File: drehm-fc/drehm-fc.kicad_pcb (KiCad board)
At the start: 2 copper layers, 18 parts, among them J1 TSW-113-08-T-T-RA, J4 Conn_01x04, U1 DEV-15583

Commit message: design rules set, teensy footprint modified
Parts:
- removed TP1, TP2: TestPoint, TestPoint:TestPoint_Pad_4.0x4.0mm
- J4: footprint Connector_PinHeader_2.54mm:PinHeader_1x04_P2.54mm_Horizontal -> Connector_PinHeader_2.54mm:PinHeader_1x04_P2.54mm_Vertical
- moved MT1 51.9 mm to (152.1, 122.2), turned to 180 degrees
- moved R1 42.7 mm to (151.7, 124.2)
- moved C2 42.0 mm to (153.9, 119.6), turned to 90 degrees
- moved R2 41.7 mm to (153.2, 124.7), turned to 180 degrees
- moved C3 40.5 mm to (154.7, 119.6), turned to 90 degrees
- moved C1 36.6 mm to (152.8, 112.5), turned to 180 degrees
- moved J1 17.3 mm to (127.7, 126.4), turned to -90 degrees
- moved J4 15.6 mm to (159.2, 113.7)
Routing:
- net /UART RX/I2C SCL: track 0.00 -> 20.9 mm
- net /UART TX/I2C SDA: track 0.00 -> 15.2 mm
- net +3V3: track 0.00 -> 3.12 mm

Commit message: IMU Routing finished, board outline done
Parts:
- moved H1 80.5 mm to (125.0, 147.0)
- moved FID1 70.5 mm to (129.5, 147.0)
- moved H3 69.0 mm to (159.0, 147.0)
- moved H2 36.1 mm to (159.0, 103.0)
- moved FID2 25.0 mm to (154.5, 103.0)
- moved FID3 22.2 mm to (129.5, 103.0)
- moved H4 18.4 mm to (125.0, 103.0)
- moved C1 14.9 mm to (150.1, 127.2), turned to 90 degrees
- moved C3 12.1 mm to (151.0, 131.1), turned to 180 degrees
- moved C2 11.1 mm to (151.0, 130.3), turned to 180 degrees
- moved MT1 5.87 mm to (152.0, 128.0), turned to -90 degrees
- moved R1 4.76 mm to (154.0, 128.4), turned to 90 degrees
- moved J1 2.33 mm to (130.0, 126.4)
- moved R2 2.30 mm to (154.0, 126.9), turned to -90 degrees
- moved J4 0.25 mm to (159.5, 113.7)
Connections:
- J1 pad 36: (no net) -> Net-(J1-Pad36)
- J1 pad 39: (no net) -> Net-(J1-Pad39)
- U1 pad 11: Net-(J1A-36) -> Net-(J1-Pad36)
- U1 pad 12: Net-(J1A-39) -> Net-(J1-Pad39)
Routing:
- net /+5V: track 0.00 -> 56.4 mm
- net +3V3: track 3.12 -> 56.3 mm
- net INT2: track 0.00 -> 20.0 mm, vias 0 -> 2
- net INT1: track 0.00 -> 13.5 mm
- net /IMU_SDA: track 0.00 -> 10.7 mm
- net Earth: track 0.00 -> 6.84 mm, vias 0 -> 6
- net Net-(J1-Pad39): track 0.00 -> 3.09 mm
- net Net-(J1-Pad36): track 0.00 -> 3.09 mm
- net Net-(J1-Pad33): track 0.00 -> 3.09 mm
- net Net-(J1-Pad30): track 0.00 -> 3.09 mm
- net Net-(J1-Pad27): track 0.00 -> 3.09 mm
- net Net-(J1-Pad24): track 0.00 -> 3.09 mm
- net Net-(J1-Pad21): track 0.00 -> 3.09 mm
- net Net-(J1-Pad18): track 0.00 -> 3.09 mm
- net Net-(J1-Pad15): track 0.00 -> 3.09 mm
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- added copper zone on F.Cu, net +3V3
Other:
- board outline added: 40.5 x 50.5 mm

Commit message: Routing mostly done, finishing touches WIP
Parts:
- moved J4 36.7 mm to (140.9, 145.3), turned to 90 degrees
- moved H3 3.48 mm to (155.6, 146.6)
- moved FID2 3.45 mm to (151.1, 103.0)
- moved H2 3.45 mm to (155.6, 103.0)
- moved FID1 0.90 mm to (130.2, 146.5)
- moved H1 0.90 mm to (125.8, 146.5)
- moved FID3 0.75 mm to (130.2, 103.0)
- moved H4 0.75 mm to (125.8, 103.0)
- moved C3 0.06 mm to (151.0, 131.2)
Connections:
- J1 pad 01: Net-(J1-Pad01) -> Earth
- J1 pad 04: Net-(J1-Pad01) -> Earth
- J1 pad 07: Net-(J1-Pad01) -> Earth
- J1 pad 10: Net-(J1-Pad01) -> Earth
- J1 pad 13: Net-(J1-Pad01) -> Earth
- J1 pad 16: Net-(J1-Pad01) -> Earth
- J1 pad 19: Net-(J1-Pad01) -> Earth
- J1 pad 22: Net-(J1-Pad01) -> Earth
- J1 pad 25: Net-(J1-Pad01) -> Earth
- J1 pad 28: Net-(J1-Pad01) -> Earth
- J1 pad 31: Net-(J1-Pad01) -> Earth
- J1 pad 34: Net-(J1-Pad01) -> Earth
- J1 pad 37: Net-(J1-Pad01) -> Earth
- U1 pad G1: Net-(J1-Pad01) -> Earth
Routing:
- net +3V3: track 56.3 -> 73.1 mm
- net Earth: track 6.84 -> 22.8 mm, vias 6 -> 19
- net /UART TX/I2C SDA: track 16.2 -> 18.0 mm
- net /IMU_SCL: track 2.81 -> 3.90 mm
- net /UART RX/I2C SCL: track 21.1 -> 22.1 mm
- added copper zone on B.Cu, net Earth
- added copper zone on F.Cu, net Earth
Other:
- board size 40.5 x 50.5 mm -> 36.3 x 50 mm
- board text added: "+"
- board text added: "+3.3v"
- board text added: "+5V"
- board text added: "-"
- board text added: "GND"

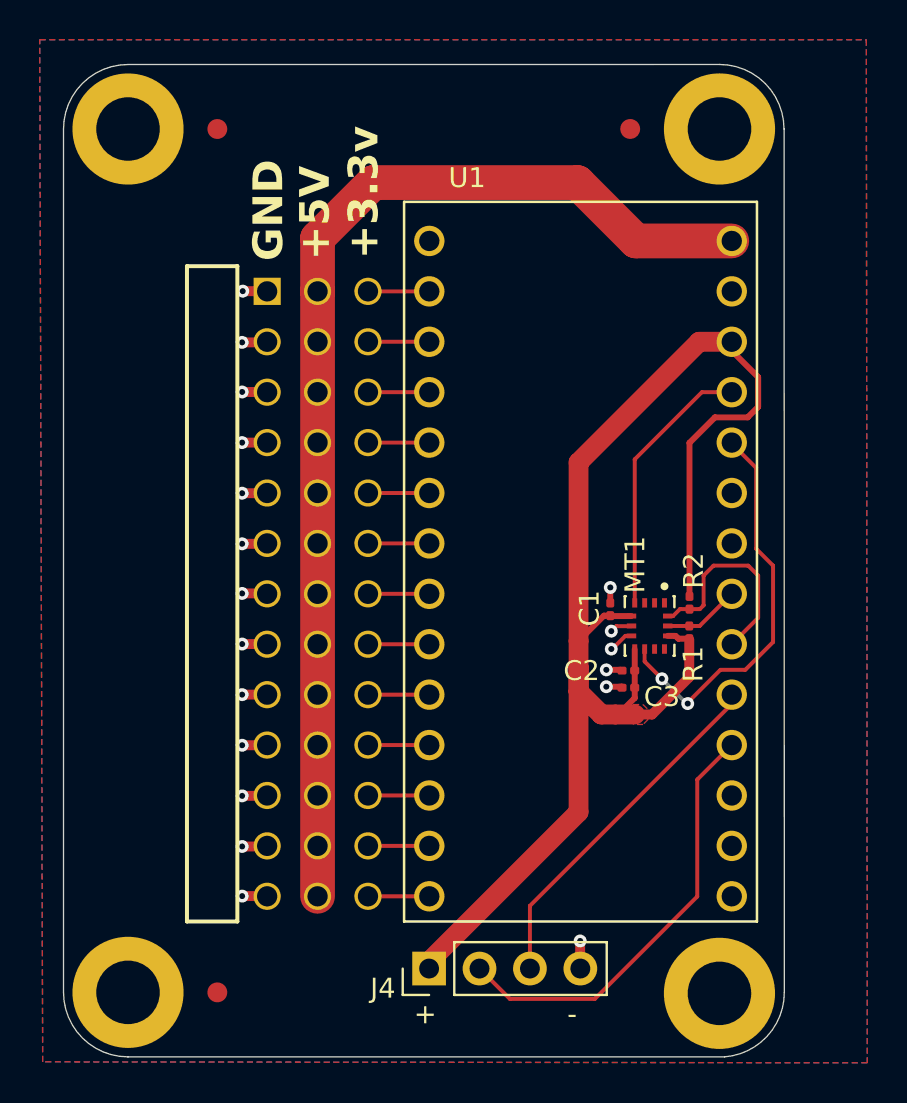
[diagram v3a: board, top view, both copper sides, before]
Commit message: Manufacturability changes, silkscreen update
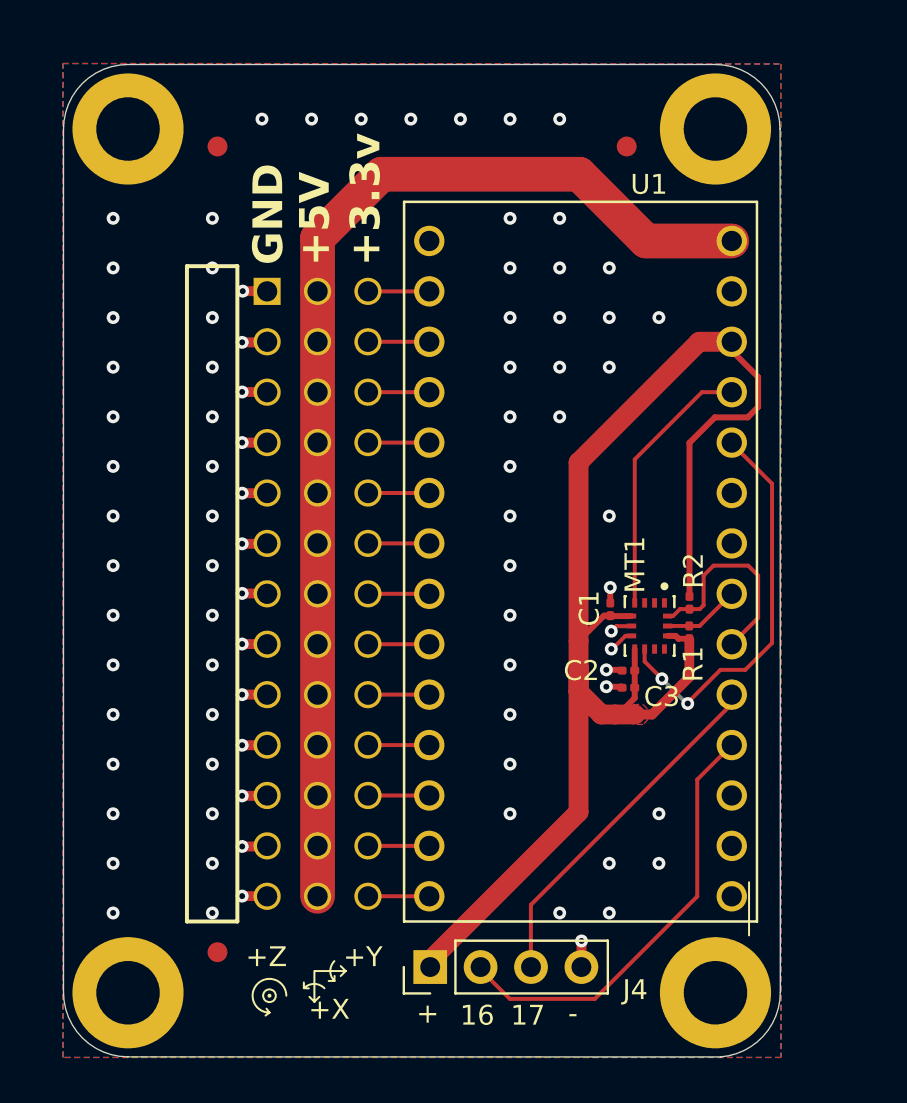
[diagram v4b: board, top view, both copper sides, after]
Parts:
- moved FID1 2.02 mm to (130.3, 144.5)
- moved FID2 0.90 mm to (150.9, 103.9)
- moved FID3 0.88 mm to (130.3, 103.9)
- moved H3 0.20 mm to (155.3, 146.5)
- moved H2 0.20 mm to (155.3, 103.0)
- moved J4 0.09 mm to (141.0, 145.2)
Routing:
- net Earth: vias 19 -> 84
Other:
- board size 36.3 x 50 mm -> 36.1 x 50 mm
- board text added: "+X"
- board text added: "+Y"
- board text added: "+Z"
- board text added: "16"
- board text added: "17"
- board text added: "{ "ViaStitching": "0.2", "stitch_zone_0": { "HSpacing": ".5", "VSpacing": ".5", "Clearance": "0", "Randomize": false } }"
- board text added: "{ "ViaStitching": "0.2", "stitch_zone_0": { "HSpacing": "1", "VSpacing": "1", "Clearance": "0", "Randomize": false } }"

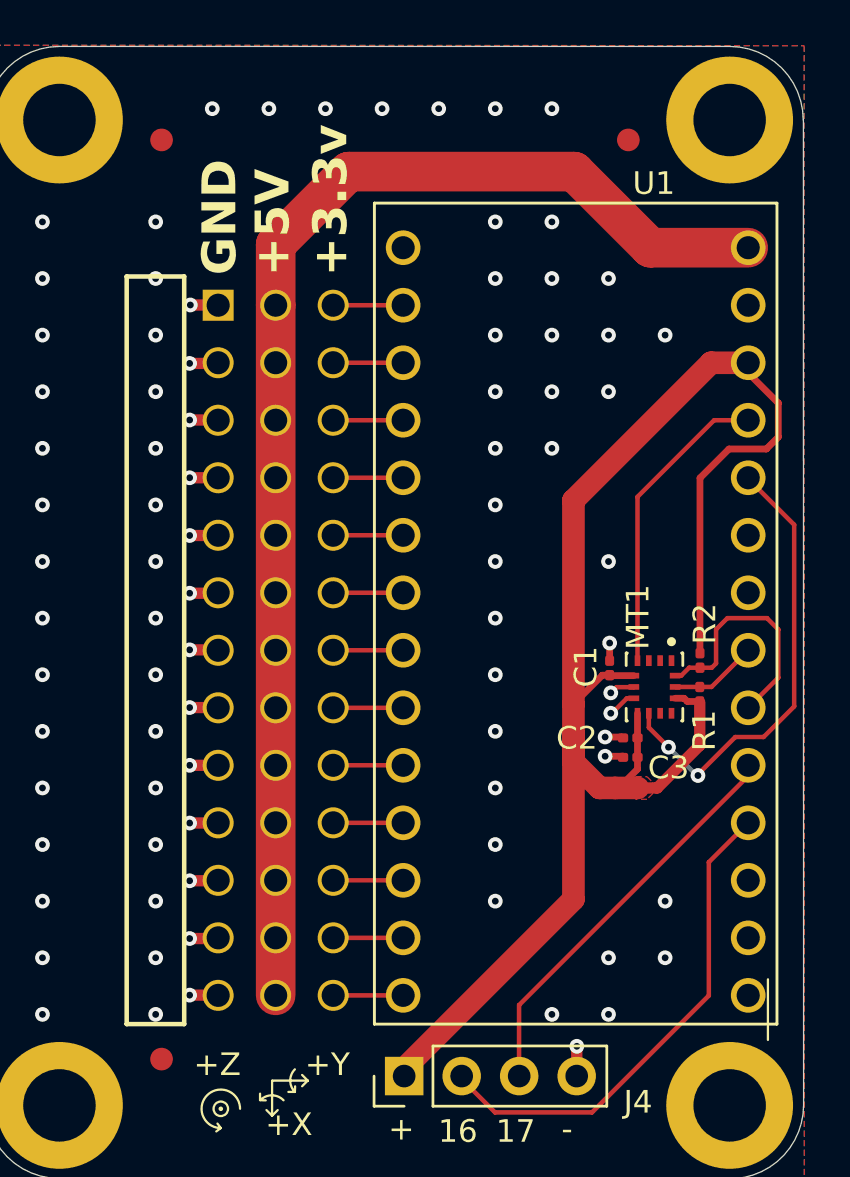
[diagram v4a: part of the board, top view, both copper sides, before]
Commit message: name and rev on silkscreen
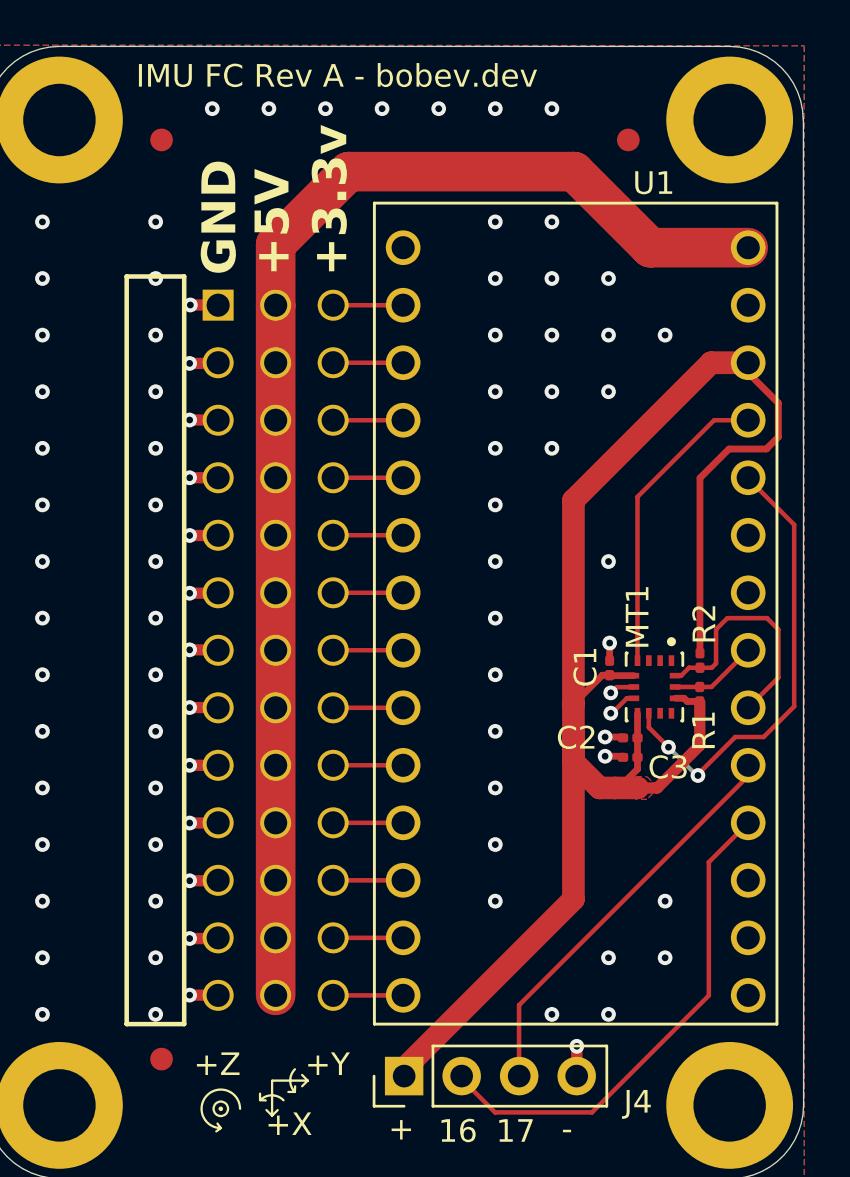
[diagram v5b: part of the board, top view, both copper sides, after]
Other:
- board text added: "IMU FC Rev A - bobev.dev"
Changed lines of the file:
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@@
-		(layer "F.SilkS")
-	)
-	(gr_line
-		(start 157.04 143.63)
-		(end 157.04 140.95)
-		(stroke
-			(width 0.1)
-			(type default)
-		)
 		(layer "F.SilkS")
 	)
@@
 		(layer "F.SilkS")
 		(effects
+			(font
+				(size 1 1)
+				(thickness 0.1)
+			)
+			(justify left bottom)
+		)
+	)
+	(gr_text "IMU FC Rev A - bobev.dev"
+		(at 129.125 101.65 0)
+		(layer "F.SilkS")
+		(effects

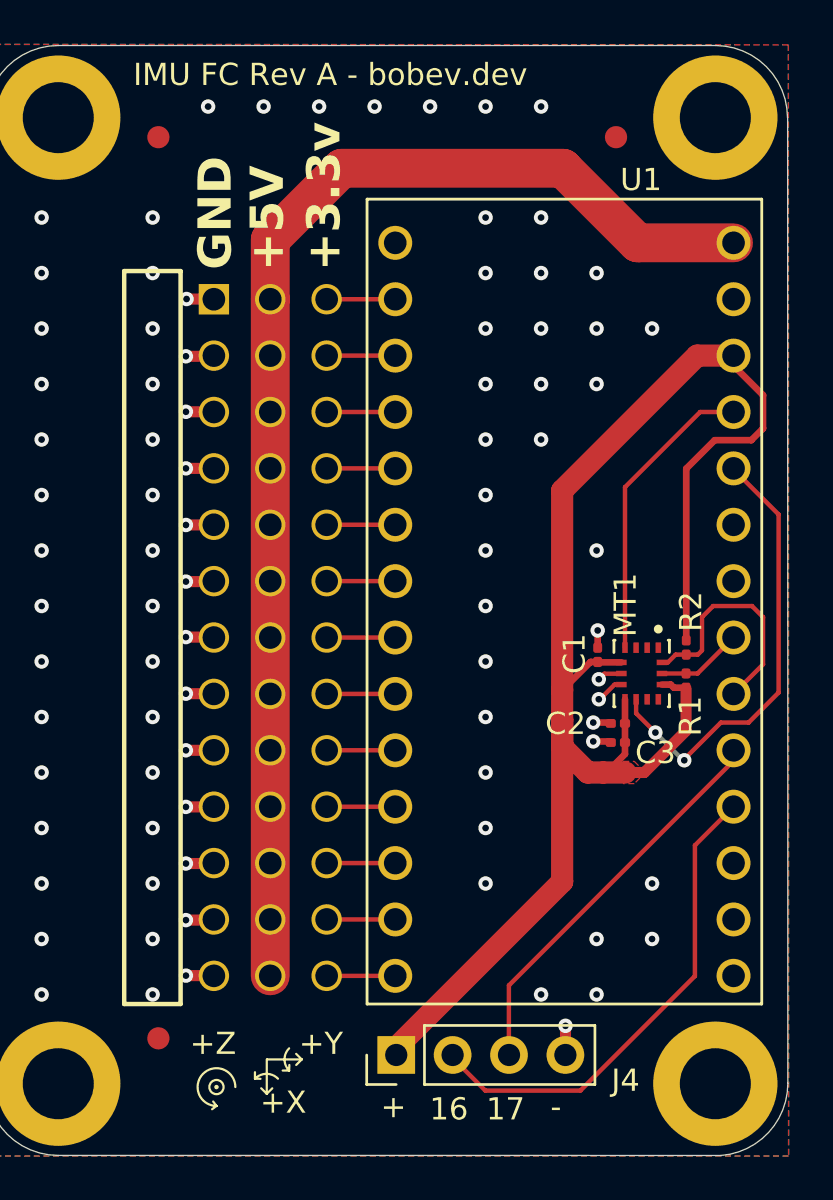
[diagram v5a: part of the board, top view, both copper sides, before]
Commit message: 0402 conversion, added holes for PCBA
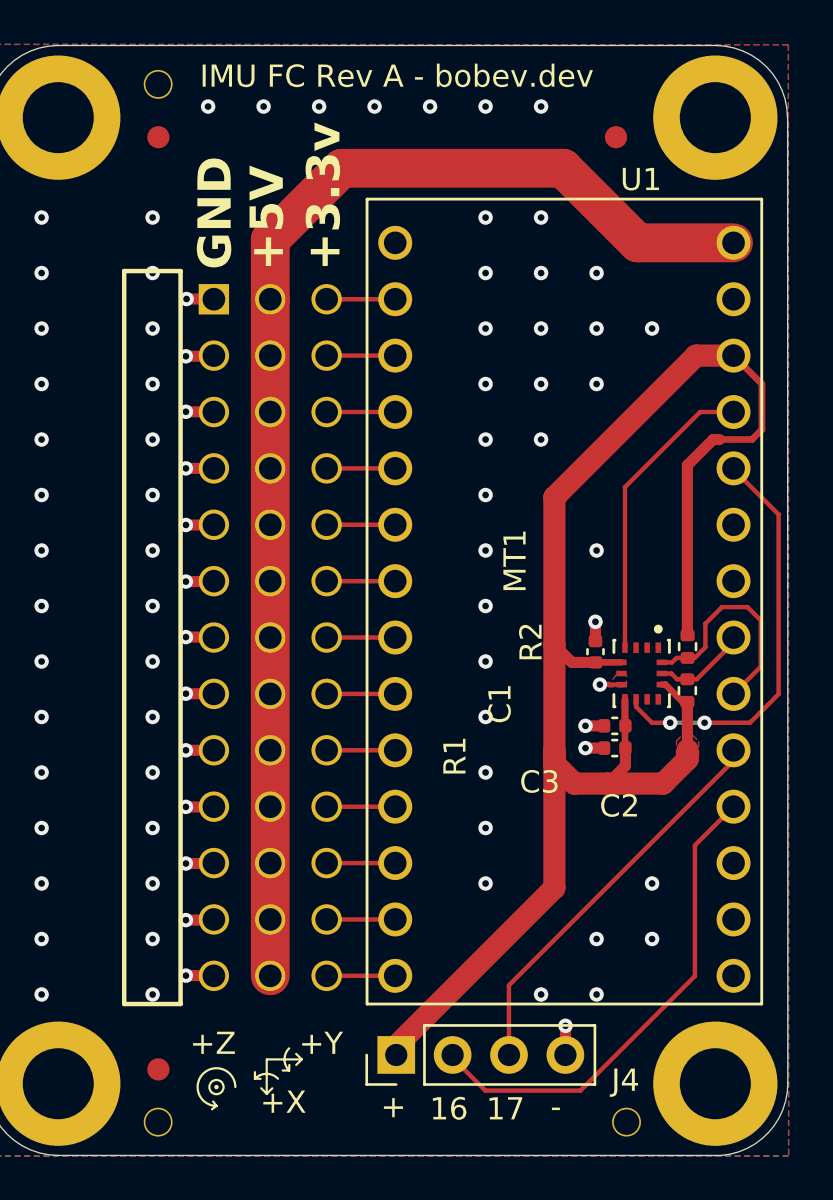
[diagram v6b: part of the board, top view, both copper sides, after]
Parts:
- added ?: , , F.Cu at (151.3, 148.2)
- added ?: , , F.Cu at (130.2, 148.2)
- added REF**: JLCPCB_MFR_Hole, JLCPCB_MFR_Hole:JLCPCB_MFR_Hole, F.Cu at (130.2, 101.5)
- C1, C2, C3: footprint Capacitor_SMD:C_0201_0603Metric -> Capacitor_SMD:C_0402_1005Metric
- R1, R2: footprint Resistor_SMD:R_0201_0603Metric -> Resistor_SMD:R_0402_1005Metric
- moved FID1 1.40 mm to (130.3, 145.9)
- moved R1 0.45 mm to (154.1, 128.8)
- moved C3 0.29 mm to (150.8, 131.4)
- moved C2 0.18 mm to (150.8, 130.4)
- moved C1 0.17 mm to (149.9, 127.1)
- moved R2 0.07 mm to (154.1, 126.8)
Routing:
- net +3V3: track 73.1 -> 75.6 mm
- net INT2: track 20.2 -> 18.6 mm
- net Earth: track 22.8 -> 21.4 mm, vias 84 -> 83
- net /IMU_SCL: track 3.90 -> 4.55 mm
- net /IMU_SDA: track 10.7 -> 10.2 mm
